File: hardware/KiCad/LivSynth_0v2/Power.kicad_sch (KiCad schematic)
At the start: 61 parts, among them J201 9V, J202 VGND, J203 Test Points, J204 3V3, J5 Barrel_Jack_Switch, Q201 AO3401A, SW6 SW_SPDT, U1 TL074, U201 TPS63070, U3 TL074, U4 TL074, U5 LM1117-3.3, U6 TL074, U7 LM13700, U8 TL074

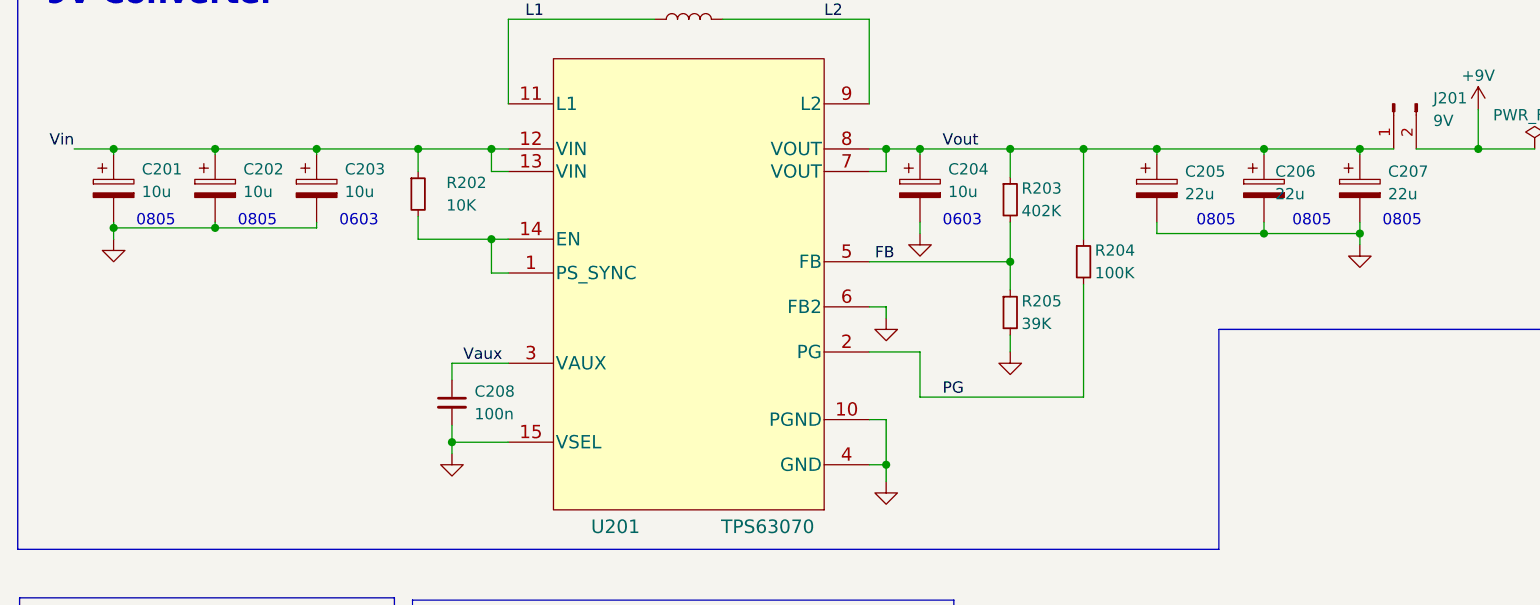
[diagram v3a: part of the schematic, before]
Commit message: LCSC component looked up
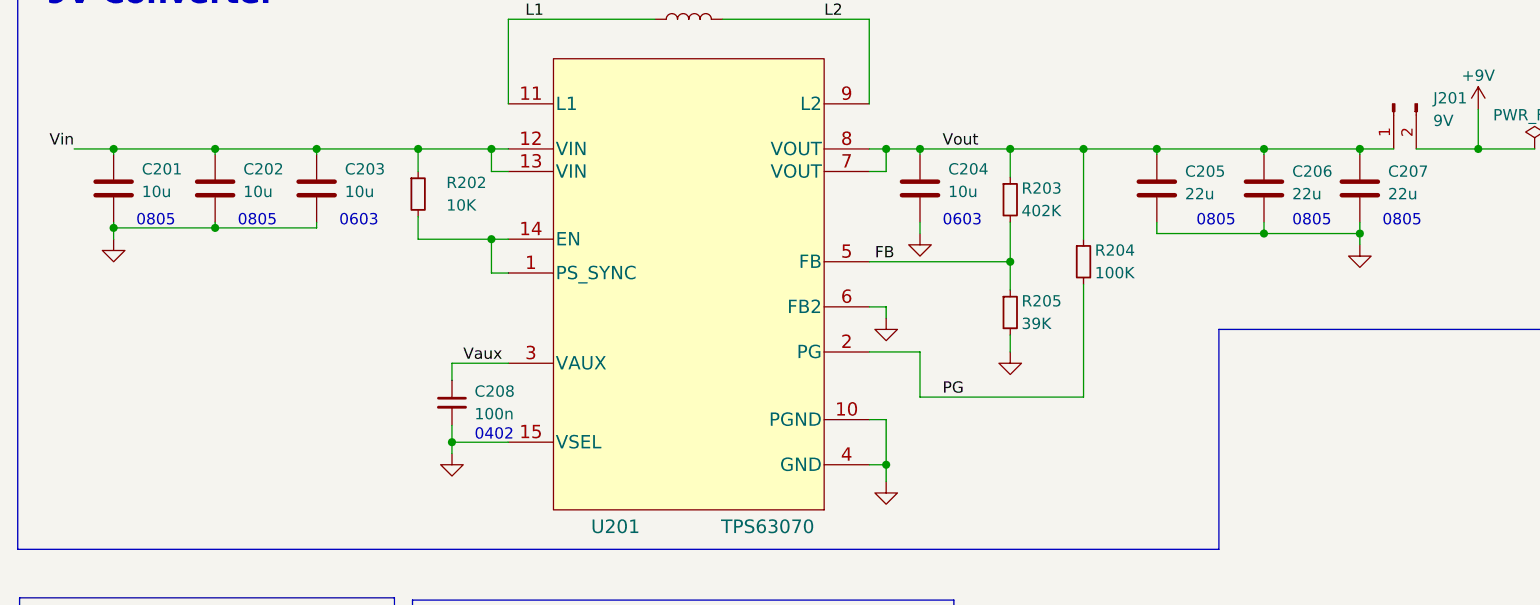
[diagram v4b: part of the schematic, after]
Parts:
- C201, C202: symbol Device:C_Polarized -> Device:C; LCSC (none) -> C109040
- C203, C204: symbol Device:C_Polarized -> Device:C; LCSC (none) -> C96446
- C205, C206, C207: symbol Device:C_Polarized -> Device:C; LCSC (none) -> C415296
- C208: footprint Capacitor_THT:C_Rect_L7.2mm_W2.5mm_P5.00mm_FKS2_FKP2_MKS2_MKP2 -> Capacitor_SMD:C_0402_1005Metric_Pad0.74x0.62mm_HandSolder; LCSC (none) -> C1523
- R202: LCSC (none) -> C25804
- R203: LCSC (none) -> C844562
- R205: LCSC (none) -> C163424
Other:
- note added: "0402"
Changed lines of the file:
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@@
+    (effects (font (size 1.27 1.27)) (justify left bottom))
+  )
+  (text "0402" (at 70.485 109.22 0)
     (effects (font (size 1.27 1.27)) (justify left bottom))
   )
@@
     (pin "2")
   )
-  (symbol (lib_id "Device:C_Polarized") (at 159.385 80.645 0) (unit 1)
-    (in_bom yes) (on_board yes)
-    (property "Reference" "C206" (id 0) (at 160.655 78.74 0)
-      (effects (font (size 1.27 1.27)) (justify left))
-    )
-    (property "Value" "22u" (id 1) (at 160.655 81.28 0)
+  (symbol (lib_id "Device:C") (at 159.385 80.645 0) (unit 1)
+    (in_bom yes) (on_board yes)
+    (property "Reference" "C206" (id 0) (at 162.56 78.74 0)
+      (effects (font (size 1.27 1.27)) (justify left))
+    )
+    (property "Value" "22u" (id 1) (at 162.56 81.28 0)
       (effects (font (size 1.27 1.27)) (justify left))
     )
@@
       (effects (font (size 1.27 1.27)) hide)
     )
-    (pin "1")
-    (pin "2")
-  )
-  (symbol (lib_id "Device:C_Polarized") (at 41.275 80.645 0) (unit 1)
+    (property "LCSC" "C415296" (id 4) (at 159.385 80.645 0)
+      (effects (font (size 1.27 1.27)) hide)
+    )
+    (pin "1")
+    (pin "2")
+  )
+  (symbol (lib_id "Device:C") (at 41.275 80.645 0) (unit 1)
     (in_bom yes) (on_board yes) (fields_autoplaced)
     (property "Reference" "C202" (id 0) (at 44.45 78.4859 0)
@@
     )
     (property "Datasheet" "~" (id 3) (at 41.275 80.645 0)
+      (effects (font (size 1.27 1.27)) hide)
+    )
+    (property "LCSC" " C109040" (id 4) (at 41.275 80.645 0)
       (effects (font (size 1.27 1.27)) hide)
     )
@@
       (effects (font (size 1.27 1.27)) hide)
     )
+    (property "LCSC" " C25804" (id 4) (at 64.135 81.28 0)
+      (effects (font (size 1.27 1.27)) hide)
+    )
     (pin "1")
     (pin "2")
@@
     (pin "1")
   )
-  (symbol (lib_id "Device:C_Polarized") (at 29.845 80.645 0) (unit 1)
+  (symbol (lib_id "Device:C") (at 29.845 80.645 0) (unit 1)
     (in_bom yes) (on_board yes) (fields_autoplaced)
     (property "Reference" "C201" (id 0) (at 33.02 78.4859 0)
@@
     )
     (property "Datasheet" "~" (id 3) (at 29.845 80.645 0)
+      (effects (font (size 1.27 1.27)) hide)
+    )
+    (property "LCSC" " C109040" (id 4) (at 29.845 80.645 0)
       (effects (font (size 1.27 1.27)) hide)
     )
@@
     (pin "1")
   )
-  (symbol (lib_id "Device:C_Polarized") (at 170.18 80.645 0) (unit 1)
+  (symbol (lib_id "Device:C") (at 170.18 80.645 0) (unit 1)
     (in_bom yes) (on_board yes)
     (property "Reference" "C207" (id 0) (at 173.355 78.74 0)
@@
     )
     (property "Datasheet" "~" (id 3) (at 170.18 80.645 0)
+      (effects (font (size 1.27 1.27)) hide)
+    )
+    (property "LCSC" "C415296" (id 4) (at 170.18 80.645 0)
       (effects (font (size 1.27 1.27)) hide)
     )
@@
     (pin "2")
   )
-  (symbol (lib_id "Device:C_Polarized") (at 52.705 80.645 0) (unit 1)
+  (symbol (lib_id "Device:C") (at 52.705 80.645 0) (unit 1)
     (in_bom yes) (on_board yes) (fields_autoplaced)
     (property "Reference" "C203" (id 0) (at 55.88 78.4859 0)
@@
     )
     (property "Datasheet" "~" (id 3) (at 52.705 80.645 0)
+      (effects (font (size 1.27 1.27)) hide)
+    )
+    (property "LCSC" " C96446" (id 4) (at 52.705 80.645 0)
       (effects (font (size 1.27 1.27)) hide)
     )
@@
     (pin "6")
   )
-  (symbol (lib_id "Device:C_Polarized") (at 147.32 80.645 0) (unit 1)
+  (symbol (lib_id "Device:C") (at 147.32 80.645 0) (unit 1)
     (in_bom yes) (on_board yes)
     (property "Reference" "C205" (id 0) (at 150.495 78.74 0)
@@
       (effects (font (size 1.27 1.27)) hide)
     )
+    (property "LCSC" "C415296" (id 4) (at 147.32 80.645 0)
+      (effects (font (size 1.27 1.27)) hide)
+    )
     (pin "1")
     (pin "2")
@@
       (effects (font (size 1.27 1.27)) (justify left))
     )
-    (property "Footprint" "Capacitor_THT:C_Rect_L7.2mm_W2.5mm_P5.00mm_FKS2_FKP2_MKS2_MKP2" (id 2) (at 67.945 104.775 0)
+    (property "Footprint" "Capacitor_SMD:C_0402_1005Metric_Pad0.74x0.62mm_HandSolder" (id 2) (at 67.945 104.775 0)
       (effects (font (size 1.27 1.27)) hide)
     )
@@
       (effects (font (size 1.27 1.27)) hide)
     )
+    (property "LCSC" " C1523" (id 4) (at 67.945 104.775 0)
+      (effects (font (size 1.27 1.27)) hide)
+    )
     (pin "1")
     (pin "2")
@@
     )
     (property "Datasheet" "~" (id 3) (at 130.81 81.915 0)
+      (effects (font (size 1.27 1.27)) hide)
+    )
+    (property "LCSC" " C844562" (id 4) (at 130.81 81.915 0)
       (effects (font (size 1.27 1.27)) hide)
     )
@@
     (pin "1")
   )
-  (symbol (lib_id "Device:C_Polarized") (at 120.65 80.645 0) (unit 1)
+  (symbol (lib_id "Device:C") (at 120.65 80.645 0) (unit 1)
     (in_bom yes) (on_board yes)
     (property "Reference" "C204" (id 0) (at 123.825 78.4859 0)
@@
     )
     (property "Datasheet" "~" (id 3) (at 120.65 80.645 0)
+      (effects (font (size 1.27 1.27)) hide)
+    )
+    (property "LCSC" " C96446" (id 4) (at 120.65 80.645 0)
       (effects (font (size 1.27 1.27)) hide)
     )
@@
       (effects (font (size 1.27 1.27)) hide)
     )
+    (property "LCSC" " C163424" (id 4) (at 130.81 94.615 0)
+      (effects (font (size 1.27 1.27)) hide)
+    )

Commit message: Prepare for JLC order, manual correction tps63070
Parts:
- D201: LCSC C2916263 -> C438308
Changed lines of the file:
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@@
       (effects (font (size 1.27 1.27)) hide)
     )
-    (property "LCSC" "C2916263" (id 4) (at 91.44 29.21 90)
+    (property "LCSC" " C438308" (id 4) (at 91.44 29.21 90)
       (effects (font (size 1.27 1.27)) hide)
     )

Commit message: Geographical reannotate
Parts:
- renumbered C210 to C1, C18 to C12, C12 to C16, C10 to C18, C209 to C2, C29 to C26, C28 to C27, C24 to C30, C25 to C31, C35 to C32, C34 to C33, C41 to C34, C39 to C35, C15 to C4, C20 to C49, C31 to C52, C207 to C53, C206 to C54, C205 to C55, C204 to C56, C208 to C57, C203 to C60, C202 to C63, C201 to C64, C4 to C7, D202 to D12, D201 to D4, H202 to H3, H201 to H4, H3 to H5, H4 to H6, H203 to H7, J202 to J12, J203 to J20, J204 to J24, J201 to J25, J5 to J7, L201 to L1, NT2 to NT1, Q201 to Q3, R207 to R1, R201 to R11, R202 to R115, R206 to R2, R203 to R94, R205 to R95, R204 to R96, SW6 to SW7, U201 to U12, U4 to U2, U3 to U4, U6 to U5, U8 to U6, U5 to U8

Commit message: Order placement 2023-01-29
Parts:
- renumbered J20 to J201
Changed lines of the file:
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@@
   (symbol (lib_id "Connector:Conn_01x06_Male") (at 28.194 145.796 0) (unit 1)
     (in_bom yes) (on_board yes) (fields_autoplaced)
-    (property "Reference" "J20" (id 0) (at 28.829 135.001 0))
-    (property "Value" "Test Points" (id 1) (at 28.829 137.541 0))
+    (property "Reference" "J201" (id 0) (at 28.829 135.89 0))
+    (property "Value" "Test Points" (id 1) (at 28.829 138.43 0))
     (property "Footprint" "Connector_PinHeader_2.54mm:PinHeader_1x06_P2.54mm_Vertical" (id 2) (at 28.194 145.796 0)
       (effects (font (size 1.27 1.27)) hide)

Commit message: Modify toggle switches (footprint and 3D model) Align R value designators Add JLC component placement checkup file
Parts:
- R96: LCSC (none) -> C25803
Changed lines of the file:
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@@
+      (effects (font (size 1.27 1.27)) hide)
+    )
+    (property "LCSC" "C25803" (id 4) (at 139.065 88.9 0)
       (effects (font (size 1.27 1.27)) hide)
     )
